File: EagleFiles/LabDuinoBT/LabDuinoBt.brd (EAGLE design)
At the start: 79.7 x 11.4 mm, 9 parts

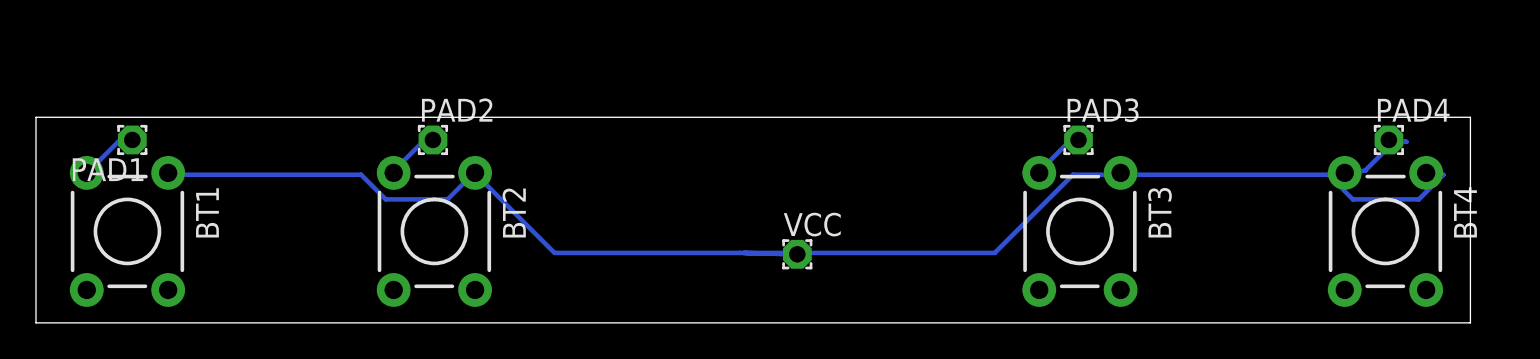
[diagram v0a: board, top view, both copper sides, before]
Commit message: Sensor Ports / Button board adjustment
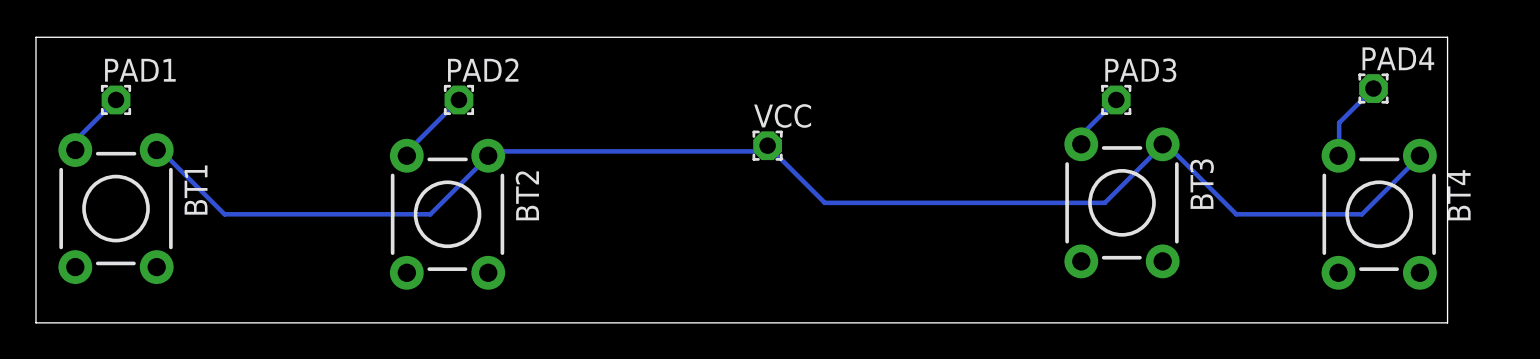
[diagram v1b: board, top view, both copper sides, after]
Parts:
- moved VCC 6.25 mm to (40.6, 9.84)
- moved PAD3 3.06 mm to (60.0, 12.4)
- moved PAD4 2.98 mm to (74.3, 13.0)
- moved BT3 2.82 mm to (60.3, 6.67)
- moved PAD2 2.65 mm to (23.5, 12.4)
- moved PAD1 2.40 mm to (4.45, 12.4), turned to 0 degrees
- moved BT1 1.42 mm to (4.45, 6.35)
- moved BT2 1.20 mm to (22.9, 6.03)
- moved BT4 1.01 mm to (74.6, 6.03)
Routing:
- net VCC: track 83.8 -> 78.8 mm
- net N$2: track 2.99 -> 4.29 mm
- net N$1: track 3.28 -> 3.96 mm
- net N$4: track 5.07 -> 4.53 mm
- net N$3: track 2.98 -> 3.51 mm
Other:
- board size 79.7 x 11.4 mm -> 78.4 x 15.9 mm

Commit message: Button Board UpDate
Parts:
- moved VCC 8.23 mm to (41.1, 1.63)
- moved BT3 2.16 mm to (58.2, 6.28)
- moved PAD3 1.55 mm to (58.5, 12.8)
- moved PAD4 1.48 mm to (75.7, 12.6)
- moved PAD2 1.21 mm to (22.4, 12.8)
- moved BT4 1.10 mm to (75.7, 6.17)
- moved BT1 0.97 mm to (5.31, 6.78)
- moved PAD1 0.89 mm to (5.22, 12.8)
- moved BT2 0.84 mm to (22.3, 6.67)
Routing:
- net VCC: track 78.8 -> 85.3 mm
- net N$3: track 3.51 -> 4.34 mm
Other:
- board size 78.4 x 15.9 mm -> 80 x 15 mm
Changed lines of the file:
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@@
 <setting verticaltext="up"/>
 </settings>
-<grid distance="0.0625" unitdist="inch" unit="inch" style="lines" multiple="1" display="no" altdistance="0.0625" altunitdist="inch" altunit="inch"/>
+<grid distance="0.5" unitdist="mm" unit="mm" style="lines" multiple="1" display="no" altdistance="0.5" altunitdist="mm" altunit="mm"/>
 <layers>
 <layer number="1" name="Top" color="4" fill="1" visible="yes" active="yes"/>
@@
 <board>
 <plain>
-<wire x1="0" y1="0" x2="78.41" y2="0" width="0" layer="20"/>
-<wire x1="78.41" y1="0" x2="78.41" y2="15.865" width="0" layer="20"/>
-<wire x1="78.41" y1="15.865" x2="0" y2="15.865" width="0" layer="20"/>
-<wire x1="0" y1="15.865" x2="0" y2="0" width="0" layer="20"/>
+<wire x1="0" y1="0" x2="80" y2="0" width="0" layer="20"/>
+<wire x1="80" y1="0" x2="80" y2="15" width="0" layer="20"/>
+<wire x1="80" y1="15" x2="0" y2="15" width="0" layer="20"/>
+<wire x1="0" y1="15" x2="0" y2="0" width="0" layer="20"/>
 </plain>
 <attributes>
@@
 </variantdefs>
 <classes>
-<class number="0" name="default" width="0" drill="0.508">
+<class number="0" name="default" width="0.381" drill="0.508">
 <clearance class="0" value="2"/>
 </class>
@@
 <description language="de">&lt;b&gt;EAGLE Design Rules&lt;/b&gt;
 &lt;p&gt;
-Die Standard-Design-Rules sind so gewÃ¤hlt, dass sie fÃ¼r
+Die Standard-Design-Rules sind so gewählt, dass sie für
 die meisten Anwendungen passen. Sollte ihre Platine
 besondere Anforderungen haben, treffen Sie die erforderlichen
@@
 <autorouter>
 <pass name="Default">
-<param name="RoutingGrid" value="12.5mil"/>
+<param name="RoutingGrid" value="50mil"/>
 <param name="AutoGrid" value="1"/>
 <param name="Efforts" value="0"/>
@@
 <param name="PrefDir.14" value="0"/>
 <param name="PrefDir.15" value="0"/>
-<param name="PrefDir.16" value="-"/>
+<param name="PrefDir.16" value="a"/>
 <param name="cfVia" value="8"/>
 <param name="cfNonPref" value="5"/>
@@
 </autorouter>
 <elements>
-<element name="BT1" library="SparkFun-Retired" package="TACTILE-PTH" value="" x="4.445" y="6.35" rot="R270"/>
-<element name="BT2" library="SparkFun-Retired" package="TACTILE-PTH" value="" x="22.86" y="6.0325" rot="R270"/>
-<element name="BT3" library="SparkFun-Retired" package="TACTILE-PTH" value="" x="60.325" y="6.6675" rot="R270"/>
-<element name="BT4" library="SparkFun-Retired" package="TACTILE-PTH" value="" x="74.6125" y="6.0325" rot="R270"/>
-<element name="PAD1" library="wirepad" package="1,6/0,9" value="" x="4.445" y="12.3825"/>
-<element name="PAD2" library="wirepad" package="1,6/0,9" value="" x="23.495" y="12.3825"/>
-<element name="PAD3" library="wirepad" package="1,6/0,9" value="" x="60.0075" y="12.3825"/>
-<element name="PAD4" library="wirepad" package="1,6/0,9" value="" x="74.295" y="13.0175"/>
-<element name="VCC" library="wirepad" package="1,6/0,9" value="" x="40.64" y="9.8425"/>
+<element name="BT1" library="SparkFun-Retired" package="TACTILE-PTH" value="" x="5.31" y="6.78" rot="R270"/>
+<element name="BT2" library="SparkFun-Retired" package="TACTILE-PTH" value="" x="22.31" y="6.67" rot="R270"/>
+<element name="BT3" library="SparkFun-Retired" package="TACTILE-PTH" value="" x="58.2" y="6.28" rot="R270"/>
+<element name="BT4" library="SparkFun-Retired" package="TACTILE-PTH" value="" x="75.7" y="6.17" rot="R270"/>
+<element name="PAD1" library="wirepad" package="1,6/0,9" value="" x="5.22" y="12.82"/>
+<element name="PAD2" library="wirepad" package="1,6/0,9" value="" x="22.37" y="12.82"/>
+<element name="PAD3" library="wirepad" package="1,6/0,9" value="" x="58.52" y="12.82"/>
+<element name="PAD4" library="wirepad" package="1,6/0,9" value="" x="75.72" y="12.63"/>
+<element name="VCC" library="wirepad" package="1,6/0,9" value="" x="41.14" y="1.63"/>
 </elements>
 <signals>
@@
 <contactref element="BT4" pad="1"/>
 <contactref element="VCC" pad="1"/>
-<wire x1="73.66" y1="6.0325" x2="76.835" y2="9.2075" width="0.254" layer="16"/>
-<wire x1="66.675" y1="6.0325" x2="73.66" y2="6.0325" width="0.254" layer="16"/>
-<wire x1="62.865" y1="9.8425" x2="66.675" y2="6.0325" width="0.254" layer="16"/>
-<wire x1="76.835" y1="9.2075" x2="76.8731" y2="9.2837" width="0.254" layer="16"/>
-<wire x1="62.865" y1="9.8425" x2="62.5856" y2="9.9187" width="0.254" layer="16"/>
-<wire x1="40.3225" y1="9.525" x2="40.64" y2="9.8425" width="0.254" layer="16"/>
-<wire x1="25.4" y1="9.525" x2="40.3225" y2="9.525" width="0.254" layer="16"/>
-<wire x1="25.4" y1="9.525" x2="25.1206" y2="9.2837" width="0.254" layer="16"/>
-<wire x1="10.4775" y1="6.0325" x2="6.985" y2="9.525" width="0.254" layer="16"/>
-<wire x1="21.9075" y1="6.0325" x2="10.4775" y2="6.0325" width="0.254" layer="16"/>
-<wire x1="25.0825" y1="9.2075" x2="21.9075" y2="6.0325" width="0.254" layer="16"/>
-<wire x1="6.985" y1="9.525" x2="6.7056" y2="9.6012" width="0.254" layer="16"/>
-<wire x1="25.0825" y1="9.2075" x2="25.1206" y2="9.2837" width="0.254" layer="16"/>
-<wire x1="59.3725" y1="6.6675" x2="62.5475" y2="9.8425" width="0.254" layer="16"/>
-<wire x1="43.815" y1="6.6675" x2="59.3725" y2="6.6675" width="0.254" layer="16"/>
-<wire x1="40.64" y1="9.8425" x2="43.815" y2="6.6675" width="0.254" layer="16"/>
-<wire x1="62.5475" y1="9.8425" x2="62.5856" y2="9.9187" width="0.254" layer="16"/>
+<wire x1="74.75" y1="6.25" x2="77.75" y2="9.25" width="0.381" layer="16"/>
+<wire x1="63.75" y1="6.25" x2="74.75" y2="6.25" width="0.381" layer="16"/>
+<wire x1="60.5" y1="9.5" x2="63.75" y2="6.25" width="0.381" layer="16"/>
+<wire x1="77.75" y1="9.25" x2="77.9606" y2="9.4212" width="0.381" layer="16"/>
+<wire x1="60.5" y1="9.5" x2="60.4606" y2="9.5312" width="0.381" layer="16"/>
+<wire x1="33" y1="9.75" x2="36.625" y2="6.125" width="0.381" layer="16"/>
+<wire x1="36.625" y1="6.125" x2="41" y2="1.75" width="0.381" layer="16"/>
+<wire x1="24.75" y1="9.75" x2="33" y2="9.75" width="0.381" layer="16"/>
+<wire x1="41" y1="1.75" x2="41.14" y2="1.63" width="0.381" layer="16"/>
+<wire x1="24.75" y1="9.75" x2="24.5706" y2="9.9212" width="0.381" layer="16"/>
+<wire x1="11" y1="6.75" x2="7.75" y2="10" width="0.381" layer="16"/>
+<wire x1="21.5" y1="6.75" x2="11" y2="6.75" width="0.381" layer="16"/>
+<wire x1="24.5" y1="9.75" x2="21.5" y2="6.75" width="0.381" layer="16"/>
+<wire x1="7.75" y1="10" x2="7.5706" y2="10.0312" width="0.381" layer="16"/>
+<wire x1="24.5" y1="9.75" x2="24.5706" y2="9.9212" width="0.381" layer="16"/>
+<wire x1="57.5" y1="6.25" x2="60.5" y2="9.25" width="0.381" layer="16"/>
+<wire x1="36.75" y1="6.25" x2="57.5" y2="6.25" width="0.381" layer="16"/>
+<wire x1="60.5" y1="9.25" x2="60.4606" y2="9.5312" width="0.381" layer="16"/>
+<wire x1="36.75" y1="6.25" x2="36.625" y2="6.125" width="0.381" layer="16"/>
 </signal>
 <signal name="N$1">
 <contactref element="BT1" pad="3"/>
 <contactref element="PAD1" pad="1"/>
-<wire x1="1.905" y1="9.8425" x2="4.445" y2="12.3825" width="0.254" layer="16"/>
-<wire x1="1.905" y1="9.8425" x2="2.1844" y2="9.6012" width="0.254" layer="16"/>
+<wire x1="5" y1="12" x2="5" y2="12.75" width="0.381" layer="16"/>
+<wire x1="3.25" y1="10.25" x2="5" y2="12" width="0.381" layer="16"/>
+<wire x1="5" y1="12.75" x2="5.22" y2="12.82" width="0.381" layer="16"/>
+<wire x1="3.25" y1="10.25" x2="3.0494" y2="10.0312" width="0.381" layer="16"/>
 </signal>
 <signal name="N$2">
 <contactref element="BT2" pad="3"/>
 <contactref element="PAD2" pad="1"/>
-<wire x1="20.6375" y1="9.525" x2="23.495" y2="12.3825" width="0.254" layer="16"/>
-<wire x1="20.6375" y1="9.525" x2="20.5994" y2="9.2837" width="0.254" layer="16"/>
+<wire x1="22.25" y1="12.25" x2="22.25" y2="12.75" width="0.381" layer="16"/>
+<wire x1="20" y1="10" x2="22.25" y2="12.25" width="0.381" layer="16"/>
+<wire x1="22.25" y1="12.75" x2="22.37" y2="12.82" width="0.381" layer="16"/>
+<wire x1="20" y1="10" x2="20.0494" y2="9.9212" width="0.381" layer="16"/>
 </signal>
 <signal name="N$3">
 <contactref element="BT3" pad="3"/>
 <contactref element="PAD3" pad="1"/>
-<wire x1="57.785" y1="10.16" x2="60.0075" y2="12.3825" width="0.254" layer="16"/>
-<wire x1="57.785" y1="10.16" x2="58.0644" y2="9.9187" width="0.254" layer="16"/>
+<wire x1="56" y1="10.25" x2="58.5" y2="12.75" width="0.381" layer="16"/>
+<wire x1="56" y1="9.75" x2="56" y2="10.25" width="0.381" layer="16"/>
+<wire x1="58.5" y1="12.75" x2="58.52" y2="12.82" width="0.381" layer="16"/>
+<wire x1="56" y1="9.75" x2="55.9394" y2="9.5312" width="0.381" layer="16"/>
 </signal>
 <signal name="N$4">
 <contactref element="BT4" pad="3"/>
 <contactref element="PAD4" pad="1"/>
-<wire x1="72.39" y1="11.1125" x2="74.295" y2="13.0175" width="0.254" layer="16"/>
-<wire x1="72.39" y1="9.525" x2="72.39" y2="11.1125" width="0.254" layer="16"/>
-<wire x1="72.39" y1="9.525" x2="72.3519" y2="9.2837" width="0.254" layer="16"/>
+<wire x1="75.5" y1="11.5" x2="75.5" y2="12.5" width="0.381" layer="16"/>
+<wire x1="73.5" y1="9.5" x2="75.5" y2="11.5" width="0.381" layer="16"/>
+<wire x1="75.5" y1="12.5" x2="75.72" y2="12.63" width="0.381" layer="16"/>
+<wire x1="73.5" y1="9.5" x2="73.4394" y2="9.4212" width="0.381" layer="16"/>
 </signal>
 </signals>
